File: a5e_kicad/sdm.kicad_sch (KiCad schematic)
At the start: 27 parts, among them IC201 74AVC1T45GM-Q100H, IC202 74AVC1T45GM-Q100H, U1 A5EB013B-B23B, U201 MT25QU256ABB8E12-0SIT

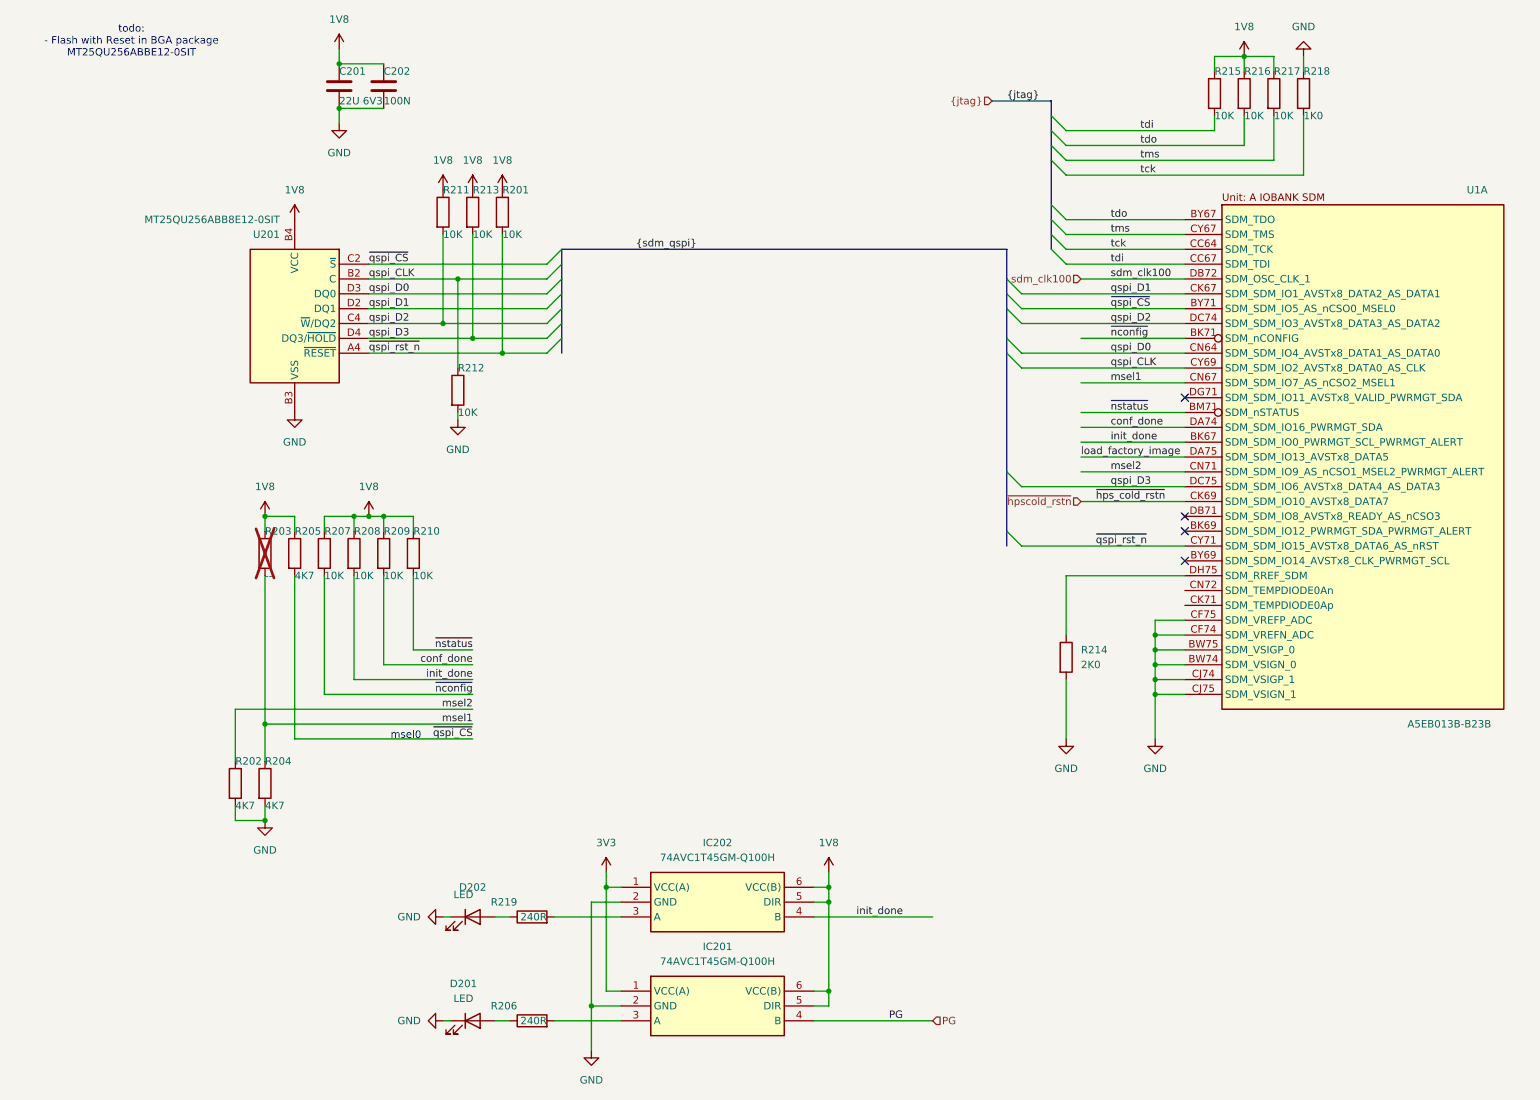
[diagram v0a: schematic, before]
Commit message: add vias to lppdr balls
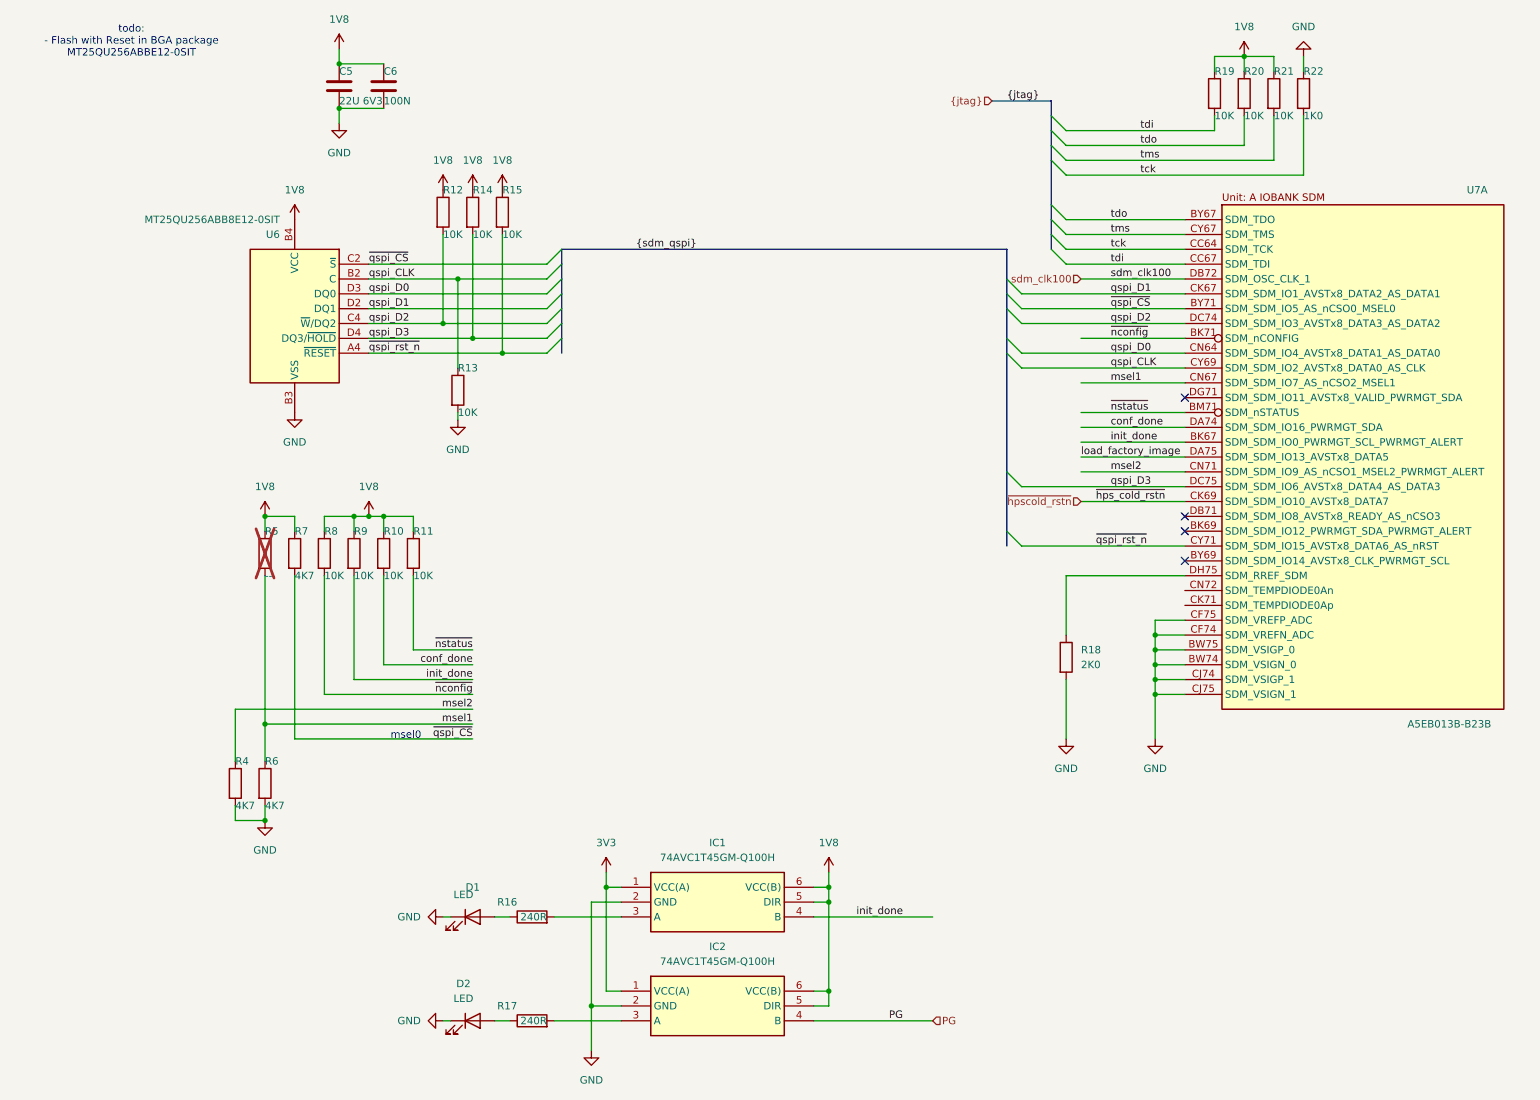
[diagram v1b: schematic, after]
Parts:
- renumbered C201 to C5, C202 to C6, D202 to D1, D201 to D2, IC202 to IC1, IC201 to IC2, R209 to R10, R210 to R11, R211 to R12, R212 to R13, R213 to R14, R201 to R15, R219 to R16, R206 to R17, R214 to R18, R215 to R19, R216 to R20, R217 to R21, R218 to R22, R202 to R4, R203 to R5, R204 to R6, R205 to R7, R207 to R8, R208 to R9, U201 to U6, U1 to U7

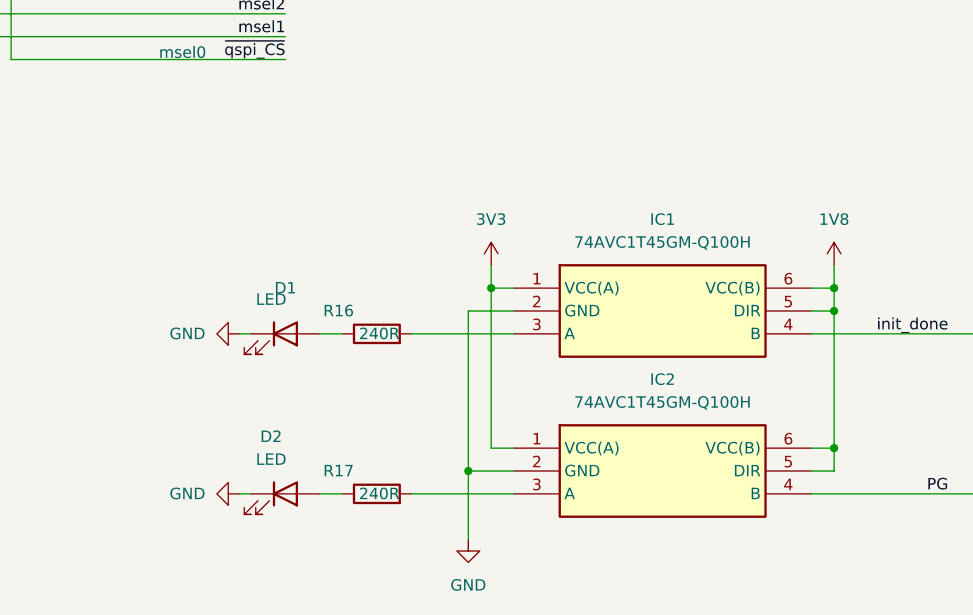
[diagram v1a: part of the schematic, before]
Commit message: add another powersupply for lpddr4
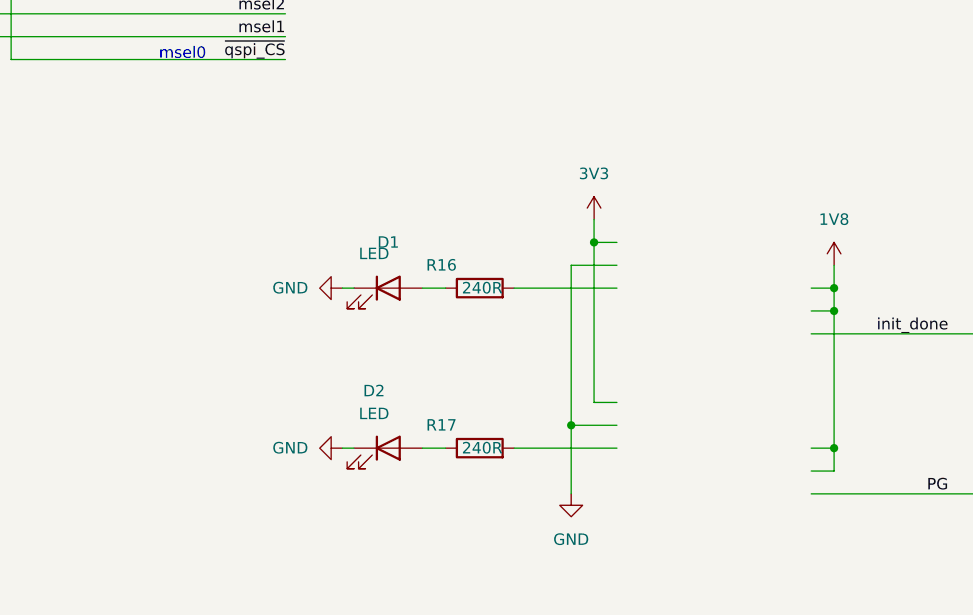
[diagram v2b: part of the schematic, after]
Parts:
- removed IC1, IC2: 74AVC1T45GM-Q100H, symbol 74AVC1T45GM-Q100H:74AVC1T45GM-Q100H
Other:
- moved on the sheet: D1, D2, R16, R17

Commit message: savegame, after fixing wird problems with schematic sync
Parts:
- removed R5: --, Resistor_SMD:R_0402_1005Metric, symbol Device:R
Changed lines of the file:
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@@
-	)
-	(symbol
-		(lib_id "Device:R")
-		(at 53.34 105.41 0)
-		(unit 1)
-		(body_style 1)
-		(exclude_from_sim no)
-		(in_bom no)
-		(on_board yes)
-		(in_pos_files yes)
-		(dnp yes)
-		(property "Reference" "R5"
-			(at 53.34 101.6 0)
-			(show_name no)
-			(do_not_autoplace no)
-			(effects
-				(font
-					(size 1.27 1.27)
-				)
-				(justify left)
-			)
-		)
-		(property "Value" "--"
-			(at 53.34 109.22 0)
-			(show_name no)
-			(do_not_autoplace no)
-			(effects
-				(font
-					(size 1.27 1.27)
-				)
-				(justify left)
-			)
-		)
-		(property "Footprint" "Resistor_SMD:R_0402_1005Metric"
-			(at 51.562 105.41 90)
-			(hide yes)
-			(show_name no)
-			(do_not_autoplace no)
-			(effects
-				(font
-					(size 1.27 1.27)
-				)
-			)
-		)
-		(property "Datasheet" ""
-			(at 53.34 105.41 0)
-			(hide yes)
-			(show_name no)
-			(do_not_autoplace no)
-			(effects
-				(font
-					(size 1.27 1.27)
-				)
-			)
-		)
-		(property "Description" "Resistor"
-			(at 53.34 105.41 0)
-			(hide yes)
-			(show_name no)
-			(do_not_autoplace no)
-			(effects
-				(font
-					(size 1.27 1.27)
-				)
-			)
-		)
-		(pin "2"
-		)
-		(pin "1"
-		)
-		(instances
-			(project "DBM_A5E013"
-				(path "/267d02d2-570f-41a1-8015-b378cedbc665/8aaf6c2b-ae6e-4499-806d-67948f95803c"
-					(reference "R203")
-					(unit 1)
-				)
-			)
-			(project "agilex_3_soc"
-				(path "/a5b98d95-6877-4284-904f-d04e32723ae0/8aaf6c2b-ae6e-4499-806d-67948f95803c"
-					(reference "R5")
-					(unit 1)
-				)
-			)
-		)
 	)
 	(symbol

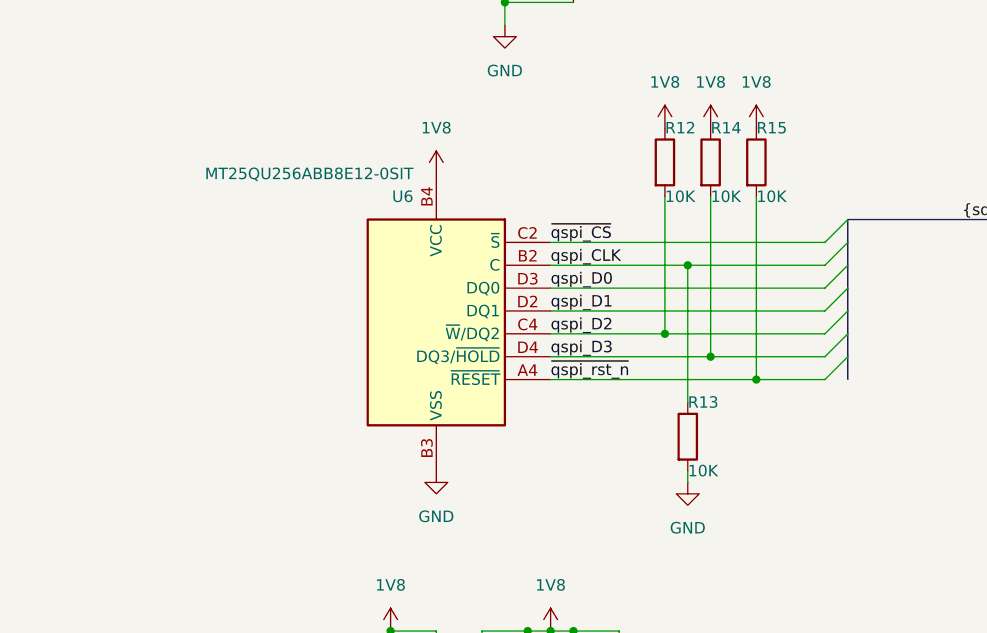
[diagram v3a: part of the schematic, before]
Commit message: add qspi
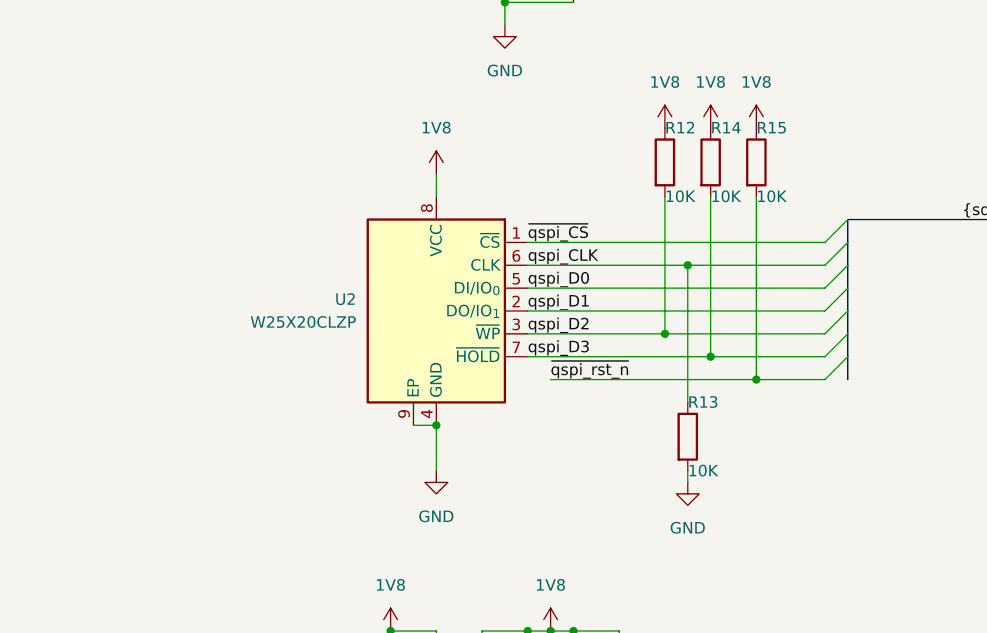
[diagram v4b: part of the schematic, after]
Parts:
- removed U6: MT25QU256ABB8E12-0SIT, Hyperram:BGA25C100P5X5_800X600X120N, symbol RR_LIB_DBM_A5E:MT25QU256ABB8E12-0SIT
- added U2: W25X20CLZP, Package_SON:WSON-8-1EP_6x5mm_P1.27mm_EP3.4x4.3mm, symbol Memory_Flash:W25X20CLZP
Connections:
- net 1V8: now also U2.8 (VCC)
- net GND: now also U2.4 (GND), U2.9 (EP)
- net qspi_CLK: now also U2.6 (CLK)
- net qspi_D0: now also U2.5 (DI/IO_{0})
- net qspi_D1: now also U2.2 (DO/IO_{1})
- net qspi_D2: now also U2.3 (~{WP})
- net qspi_D3: now also U2.7 (~{HOLD})
- net ~{qspi_CS}: now also U2.1 (~{CS})
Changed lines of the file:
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@@
 	)
 	(junction
+		(at 58.42 76.2)
+		(diameter 0)
+		(color 0 0 0 0)
+	)
+	(junction
 		(at 123.19 157.48)
 		(diameter 0)
@@
 	)
 	(junction
+		(at 86.36 58.42)
+		(diameter 0)
+		(color 0 0 0 0)
+	)
+	(junction
 		(at 205.74 124.46)
 		(diameter 0)
@@
 	)
 	(junction
-		(at 86.36 58.42)
-		(diameter 0)
-		(color 0 0 0 0)
-	)
-	(junction
 		(at 66.04 21.59)
 		(diameter 0)
@@
 	)
 	(junction
-		(at 88.9 68.58)
+		(at 53.34 134.62)
 		(diameter 0)
 		(color 0 0 0 0)
 	)
 	(junction
-		(at 53.34 134.62)
+		(at 53.34 151.13)
 		(diameter 0)
 		(color 0 0 0 0)
 	)
 	(junction
-		(at 53.34 151.13)
+		(at 88.9 68.58)
 		(diameter 0)
 		(color 0 0 0 0)
@@
 	(wire
 		(pts
+			(xy 55.88 76.2) (xy 58.42 76.2)
+		)
+		(stroke
+			(width 0)
+			(type default)
+		)
+	)
+	(wire
+		(pts
 			(xy 226.06 20.32) (xy 226.06 22.86)
 		)
@@
 	(wire
 		(pts
-			(xy 71.12 55.88) (xy 101.6 55.88)
+			(xy 68.58 55.88) (xy 101.6 55.88)
 		)
 		(stroke
@@
 	(wire
 		(pts
-			(xy 71.12 58.42) (xy 86.36 58.42)
+			(xy 68.58 58.42) (xy 86.36 58.42)
 		)
 		(stroke
@@
 	(wire
 		(pts
-			(xy 71.12 66.04) (xy 83.82 66.04)
+			(xy 68.58 66.04) (xy 83.82 66.04)
 		)
 		(stroke
@@
 	(wire
 		(pts
-			(xy 71.12 68.58) (xy 88.9 68.58)
+			(xy 68.58 68.58) (xy 88.9 68.58)
 		)
 		(stroke
@@
 	(wire
 		(pts
-			(xy 71.12 63.5) (xy 101.6 63.5)
-		)
-		(stroke
-			(width 0)
-			(type default)
-		)
-	)
-	(wire
-		(pts
 			(xy 53.34 148.59) (xy 53.34 151.13)
 		)
@@
 	(wire
 		(pts
+			(xy 58.42 76.2) (xy 58.42 81.28)
+		)
+		(stroke
+			(width 0)
+			(type default)
+		)
+	)
+	(wire
+		(pts
 			(xy 88.9 124.46) (xy 73.66 124.46)
 		)
@@
 		)
 	)
+	(wire
+		(pts
+			(xy 58.42 48.26) (xy 58.42 50.8)
+		)
+		(stroke
+			(width 0)
+			(type default)
+		)
+	)
 	(bus
 		(pts
@@
 	(wire
 		(pts
+			(xy 68.58 63.5) (xy 101.6 63.5)
+		)
+		(stroke
+			(width 0)
+			(type default)
+		)
+	)
+	(wire
+		(pts
 			(xy 53.34 99.06) (xy 58.42 99.06)
 		)
@@
 	(wire
 		(pts
-			(xy 71.12 60.96) (xy 101.6 60.96)
+			(xy 68.58 60.96) (xy 101.6 60.96)
 		)
 		(stroke
@@
 	)
 	(label "qspi_D1"
-		(at 71.12 63.5 0)
+		(at 68.58 63.5 0)
 		(effects
 			(font
@@
 	)
 	(label "~{qspi_CS}"
-		(at 71.12 55.88 0)
+		(at 68.58 55.88 0)
 		(effects
 			(font
@@
 	)
 	(label "qspi_D2"
-		(at 71.12 66.04 0)
+		(at 68.58 66.04 0)
 		(effects
 			(font
@@
 	)
 	(label "qspi_D0"
-		(at 71.12 60.96 0)
+		(at 68.58 60.96 0)
 		(effects
 			(font
@@
 	)
 	(label "qspi_CLK"
-		(at 71.12 58.42 0)
+		(at 68.58 58.42 0)
 		(effects
 			(font
@@
 	)
 	(label "qspi_D3"
-		(at 71.12 68.58 0)
+		(at 68.58 68.58 0)
 		(effects
 			(font
@@
 	)
 	(symbol
-		(lib_id "RR_LIB_DBM_A5E:MT25QU256ABB8E12-0SIT")
-		(at 58.42 63.5 0)
-		(mirror y)
-		(unit 1)
-		(body_style 1)
-		(exclude_from_sim no)
-		(in_bom yes)
-		(on_board yes)
-		(in_pos_files yes)
-		(dnp no)
-		(property "Reference" "U6"
-			(at 55.88 50.8 0)
-			(show_name no)
-			(do_not_autoplace no)
-			(effects
-				(font
-					(size 1.27 1.27)
-				)
-				(justify left)
-			)
-		)
-		(property "Value" "MT25QU256ABB8E12-0SIT"
-			(at 55.88 48.26 0)
-			(show_name no)
-			(do_not_autoplace no)
-			(effects
-				(font
-					(size 1.27 1.27)
-				)
-				(justify left)
-			)
-		)
-		(property "Footprint" "Hyperram:BGA25C100P5X5_800X600X120N"
-			(at 38.1 60.96 0)
-			(hide yes)
-			(show_name no)
-			(do_not_autoplace no)
-			(effects
-				(font
-					(size 1.27 1.27)
-				)
-			)
-		)
-		(property "Datasheet" "https://media-www.micron.com/-/media/client/global/documents/products/data-sheet/nor-flash/serial-nor/mt25q/die-rev-a/mt25q_qljs_u_256_aba_0.pdf"
-			(at 58.42 45.72 0)
-			(hide yes)
-			(show_name no)
-			(do_not_autoplace no)
-			(effects
-				(font
-					(size 1.27 1.27)
-				)
-			)
-		)
-		(property "Description" "Micron 256M, 1.8V Multiple I/O Serial NOR Flash Memory, BGA25"
-			(at 58.42 63.5 0)
-			(hide yes)
-			(show_name no)
-			(do_not_autoplace no)
-			(effects
-				(font
-					(size 1.27 1.27)
-				)
-			)
-		)
-		(pin "B4"
-		)
-		(pin "D3"
-		)
-		(pin "D4"
-		)
-		(pin "A4"
-		)
-		(pin "C2"
-		)
-		(pin "B2"
-		)
-		(pin "C4"
-		)
-		(pin "D2"
-		)
-		(pin "B3"
-		)
-		(instances
-			(project ""
-				(path "/267d02d2-570f-41a1-8015-b378cedbc665/8aaf6c2b-ae6e-4499-806d-67948f95803c"
-					(reference "U201")
-					(unit 1)
-				)
-			)
-			(project "agilex_3_soc"
-				(path "/a5b98d95-6877-4284-904f-d04e32723ae0/8aaf6c2b-ae6e-4499-806d-67948f95803c"
-					(reference "U6")
-					(unit 1)
-				)
-			)
-		)
-	)
-	(symbol
 		(lib_id "Device:R")
 		(at 53.34 144.78 0)
@@
 		(in_pos_files yes)
 		(dnp no)
-		(fields_autoplaced yes)
 		(property "Reference" "#PWR023"
 			(at 58.42 87.63 0)
@@
 	)
 	(symbol
+		(lib_id "Memory_Flash:W25X20CLZP")
+		(at 58.42 63.5 0)
+		(mirror y)
+		(unit 1)
+		(body_style 1)
+		(exclude_from_sim no)
+		(in_bom yes)
+		(on_board yes)
+		(in_pos_files yes)
+		(dnp no)
+		(fields_autoplaced yes)
+		(property "Reference" "U2"
+			(at 49.53 62.2299 0)
+			(show_name no)
+			(do_not_autoplace no)
+			(effects
+				(font
+					(size 1.27 1.27)
+				)
+				(justify left)
+			)
+		)
+		(property "Value" "W25X20CLZP"
+			(at 49.53 64.7699 0)
+			(show_name no)
+			(do_not_autoplace no)
+			(effects
+				(font
+					(size 1.27 1.27)
+				)
+				(justify left)
+			)
+		)
+		(property "Footprint" "Package_SON:WSON-8-1EP_6x5mm_P1.27mm_EP3.4x4.3mm"
+			(at 58.42 40.64 0)
+			(hide yes)
+			(show_name no)
+			(do_not_autoplace no)
+			(effects
+				(font
+					(size 1.27 1.27)
+				)
+			)
+		)
+		(property "Datasheet" "https://www.winbond.com/resource-files/w25x20cl_revf%2020150806.pdf"
+			(at 55.88 38.1 0)
+			(hide yes)
+			(show_name no)
+			(do_not_autoplace no)
+			(effects
+				(font
+					(size 1.27 1.27)
+				)
+			)
+		)
+		(property "Description" "2Mbit / 256KiB Serial Flash memory, Standard/Dual I/O SPI, 2.3-3.6V, WSON-8"
+			(at 58.42 63.5 0)
+			(hide yes)
+			(show_name no)
+			(do_not_autoplace no)
+			(effects
+				(font
+					(size 1.27 1.27)
+				)
+			)
+		)
+		(pin "6"
+		)
+		(pin "4"
+		)
+		(pin "8"
+		)
+		(pin "1"
+		)
+		(pin "9"
+		)
+		(pin "2"
+		)
+		(pin "5"
+		)
+		(pin "3"
+		)
+		(pin "7"
+		)
+		(instances
+			(project "agilex_3_soc"
+				(path "/a5b98d95-6877-4284-904f-d04e32723ae0/8aaf6c2b-ae6e-4499-806d-67948f95803c"
+					(reference "U2")
+					(unit 1)
+				)
+			)
+		)
+	)
+	(symbol
 		(lib_id "power:+3V3")
 		(at 58.42 48.26 0)
@@
 		(in_pos_files yes)
 		(dnp no)
-		(fields_autoplaced yes)
 		(property "Reference" "#PWR022"
 			(at 58.42 52.07 0)
